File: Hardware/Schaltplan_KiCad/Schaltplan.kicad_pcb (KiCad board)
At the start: 2 copper layers, 153 x 153 mm, 62 parts, among them IC1 LD1085V50, J1 3-106505-2, J2 USB_B_Micro, J3 Conn_01x04_Pin, J4 Conn_01x02_Pin, U1 MCP2562-E-SN, U2 FT231XS, U3 ESP32-DEVKITC-32U, U5 PCA9306DCTR

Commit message: completed tracing of pcb
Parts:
- moved D4 7.00 mm to (157.4, 74.5), turned to 180 degrees
- moved R15 7.00 mm to (148.4, 74.5)
- moved R20 7.00 mm to (103.5, 66.5), turned to -90 degrees
- moved R21 7.00 mm to (96.5, 66.5), turned to -90 degrees
- moved D5 5.80 mm to (157.3, 68.2), turned to 180 degrees
- moved R16 5.80 mm to (148.3, 68.2)
- moved J2 1.07 mm to (163.2, 47.9)
- moved R1 0.81 mm to (143.1, 123.7), turned to 0 degrees
- turned D6 to 180 degrees
- turned D7 to 180 degrees
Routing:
- net +5V: track 0.00 -> 290.2 mm, vias 0 -> 2
- net +3V3: track 0.00 -> 195.8 mm
- net GNDREF: track 0.00 -> 111.6 mm, vias 0 -> 1
- net /FT231_RI: track 0.00 -> 101.3 mm, vias 0 -> 1
- net /ESP32_IO4: track 0.00 -> 96.9 mm, vias 0 -> 4
- net /ESP32_IO33: track 0.00 -> 90.4 mm, vias 0 -> 2
- net /FT231_RTS: track 0.00 -> 89.3 mm, vias 0 -> 1
- net /FT231_SLEEP: track 0.00 -> 85.3 mm, vias 0 -> 2
- net /FT231_CTS: track 0.00 -> 81.1 mm, vias 0 -> 1
- net /ESP32_SCL1: track 0.00 -> 72.9 mm, vias 0 -> 2
- net /CANL: track 0.00 -> 70.3 mm
- net /ESP32TX: track 0.00 -> 67.9 mm, vias 0 -> 1
- net /ESP32_IO13: track 0.00 -> 67.8 mm, vias 0 -> 1
- net /ESP32_SDA1: track 0.00 -> 66.4 mm, vias 0 -> 2
- net /ESP32_IO27: track 0.00 -> 65.6 mm, vias 0 -> 1
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- added copper zone on B.Cu, net GNDREF
- added copper zone on F.Cu, net GNDREF
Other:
- board text added: "BAT"
- board text added: "CAN Status LEDs"
- board text added: "DOWN"
- board text added: "ENTER"
- board text added: "OFF"
- board text added: "OFF/USB"
- board text added: "POWER"
- board text added: "UP"

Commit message: finishes PCB Design
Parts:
- removed BT2: 1049, battery_holder:BAT_1049
- removed C10, C9: 47pF, Capacitor_SMD:C_1812_4532Metric_Pad1.57x3.40mm_HandSolder
- removed C11: 10uF, Capacitor_SMD:C_1812_4532Metric_Pad1.57x3.40mm_HandSolder
- removed C13: C, Capacitor_SMD:C_1812_4532Metric_Pad1.57x3.40mm_HandSolder
- removed C3, C5, C7: 100nF, Capacitor_SMD:C_1812_4532Metric_Pad1.57x3.40mm_HandSolder
- removed C4, C6, C8: 4.7uF, Capacitor_SMD:C_1812_4532Metric_Pad1.57x3.40mm_HandSolder
- removed D1, D2: LED, LED:LED_OF-SMD3528WC
- removed IC1: LD1085V50, LDO:TO255P460X1020X2008-3P
- removed J2: USB_B_Micro, Connector_USB:USB_Micro-B_Amphenol_10103594-0001LF_Horizontal
- removed R20, R21, R22, R23: 10k, Resistor_SMD:R_2010_5025Metric_Pad1.40x2.65mm_HandSolder
- removed R6, R7: 270, Resistor_SMD:R_2010_5025Metric_Pad1.40x2.65mm_HandSolder
- removed S1, S2: 1103M2S3CQE2, switches:SW_1103M2S3CQE2
- removed U2: FT231XS, USB2UART:SOP63P600X175-20N
- C1: value 22uF -> 100nF; footprint Capacitor_SMD:C_1812_4532Metric_Pad1.57x3.40mm_HandSolder -> Capacitor_SMD:C_0603_1608Metric_Pad1.08x0.95mm_HandSolder
- C14, C15: footprint Capacitor_SMD:C_1812_4532Metric_Pad1.57x3.40mm_HandSolder -> Capacitor_SMD:C_0603_1608Metric_Pad1.08x0.95mm_HandSolder
- C2: value C -> 4.7uF; footprint Capacitor_SMD:C_1812_4532Metric_Pad1.57x3.40mm_HandSolder -> Capacitor_SMD:C_0603_1608Metric_Pad1.08x0.95mm_HandSolder
- J1, U1, U3: moved to B.Cu
- R1: value R -> 120R; footprint Resistor_SMD:R_2010_5025Metric_Pad1.40x2.65mm_HandSolder -> Resistor_SMD:R_0603_1608Metric_Pad0.98x0.95mm_HandSolder
- R10, R11, R12, R13, R14, R15, R16, R17, R18, R19, R8, R9: footprint Resistor_SMD:R_2010_5025Metric_Pad1.40x2.65mm_HandSolder -> Resistor_SMD:R_0603_1608Metric_Pad0.98x0.95mm_HandSolder
- R2, R3: value 27R -> 10k; footprint Resistor_SMD:R_2010_5025Metric_Pad1.40x2.65mm_HandSolder -> Resistor_SMD:R_0603_1608Metric_Pad0.98x0.95mm_HandSolder
- R4, R5: value R -> 10k; footprint Resistor_SMD:R_2010_5025Metric_Pad1.40x2.65mm_HandSolder -> Resistor_SMD:R_0603_1608Metric_Pad0.98x0.95mm_HandSolder
- moved D3 177.9 mm to (56.3, 178.2), turned to 0 degrees
- moved D5 141.3 mm to (86.1, 190.2), turned to 0 degrees
- moved D4 140.5 mm to (77.8, 190.2), turned to 0 degrees
- moved R8 130.8 mm to (87.5, 147.2), turned to -90 degrees
- moved D6 121.6 mm to (103.7, 190.0), turned to 0 degrees
- moved D7 120.3 mm to (95.0, 190.2), turned to 0 degrees
- moved C1 117.0 mm to (50.3, 93.6), turned to 90 degrees
- moved J1 94.9 mm to (60.3, 127.3)
- moved C2 94.8 mm to (55.3, 93.6), turned to 90 degrees
- moved R16 92.9 mm to (99.6, 147.2), turned to -90 degrees
- moved R15 90.8 mm to (94.1, 147.2), turned to -90 degrees
- moved R11 90.5 mm to (67.8, 171.0)
- moved R14 82.3 mm to (67.8, 166.2)
- moved J4 79.2 mm to (66.4, 134.2), turned to 180 degrees
- moved R1 76.7 mm to (66.4, 125.3), turned to 90 degrees
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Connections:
- C14 pad 1: +5V -> +3V3
- C15 pad 1: +5V -> +3V3
- C2 pad 1: /FT231_3V3_OUT -> +5V
- D6 pad 1: /ESP32_IO13 -> /ESP32_IO19
- D7 pad 1: /ESP32_IO14 -> /ESP32_IO13
- R12 pad 2: /ESP32_IO5 -> /ESP32_IO18
- R2 pad 1: /FT231_USBDM -> +5V
- R2 pad 2: /USBDM -> /ESP32_SCL1
- R3 pad 1: /USBDP -> +5V
- R3 pad 2: /FT231_USBDP -> /DISPLAY_SCL2
- R4 pad 1: /FT231_RX -> +5V
- R4 pad 2: /ESP32TX -> /DISPLAY_SDA2
- R5 pad 1: /FT231_TX -> +5V
- R5 pad 2: /ESP32RX -> /ESP32_SDA1
- U3 pad 12: /ESP32_IO14 -> unconnected-(U3-IO14-Pad12)
- U3 pad 27: /ESP32RX -> unconnected-(U3-IO16-Pad27)
- U3 pad 28: /ESP32TX -> unconnected-(U3-IO17-Pad28)
- U3 pad 29: /ESP32_IO5 -> unconnected-(U3-IO5-Pad29)
- U3 pad 30: /FT231_CTS -> /ESP32_IO18
- U3 pad 31: /FT231_RTS -> /ESP32_IO19
- U3 pad 37: /FT231_RI -> unconnected-(U3-IO23-Pad37)
- U3 pad 7: /FT231_SLEEP -> unconnected-(U3-IO32-Pad7)
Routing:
- net /ESP32_IO19: track 0.00 -> 122.8 mm, vias 0 -> 1
- net /FT231_RI: track 101.3 -> 0.00 mm, vias 1 -> 0
- net +5V: track 290.2 -> 192.7 mm, vias 2 -> 0
- net /FT231_RTS: track 89.3 -> 0.00 mm, vias 1 -> 0
- net /ESP32_IO18: track 0.00 -> 88.3 mm, vias 0 -> 1
- net /FT231_SLEEP: track 85.3 -> 0.00 mm, vias 2 -> 0
- net /FT231_CTS: track 81.1 -> 0.00 mm, vias 1 -> 0
- net GNDREF: track 111.6 -> 36.6 mm, vias 1 -> 2
- net /ESP32TX: track 67.9 -> 0.00 mm, vias 1 -> 0
- net /ESP32_IO14: track 64.8 -> 0.00 mm, vias 2 -> 0
- net /ESP32_IO13: track 67.8 -> 129.4 mm, vias 1 -> 0
- net /ESP32RX: track 61.5 -> 0.00 mm, vias 1 -> 0
- net /ESP32_IO5: track 61.0 -> 0.00 mm
- net /ESP32_IO4: track 96.9 -> 151.6 mm, vias 4 -> 0
- net Net-(D4-A): track 5.17 -> 55.0 mm, vias 0 -> 2
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- removed copper zone on B.Cu, net GNDREF
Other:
- board size 153 x 153 mm -> 72 x 138 mm
- board text removed: "BAT"
- board text removed: "CAN Status LEDs"
- board text removed: "DOWN"
- board text removed: "Display"
- board text removed: "ENTER"
- board text removed: "OFF"
- board text removed: "OFF/USB"
- board text removed: "POWER"
- board text removed: "UP"

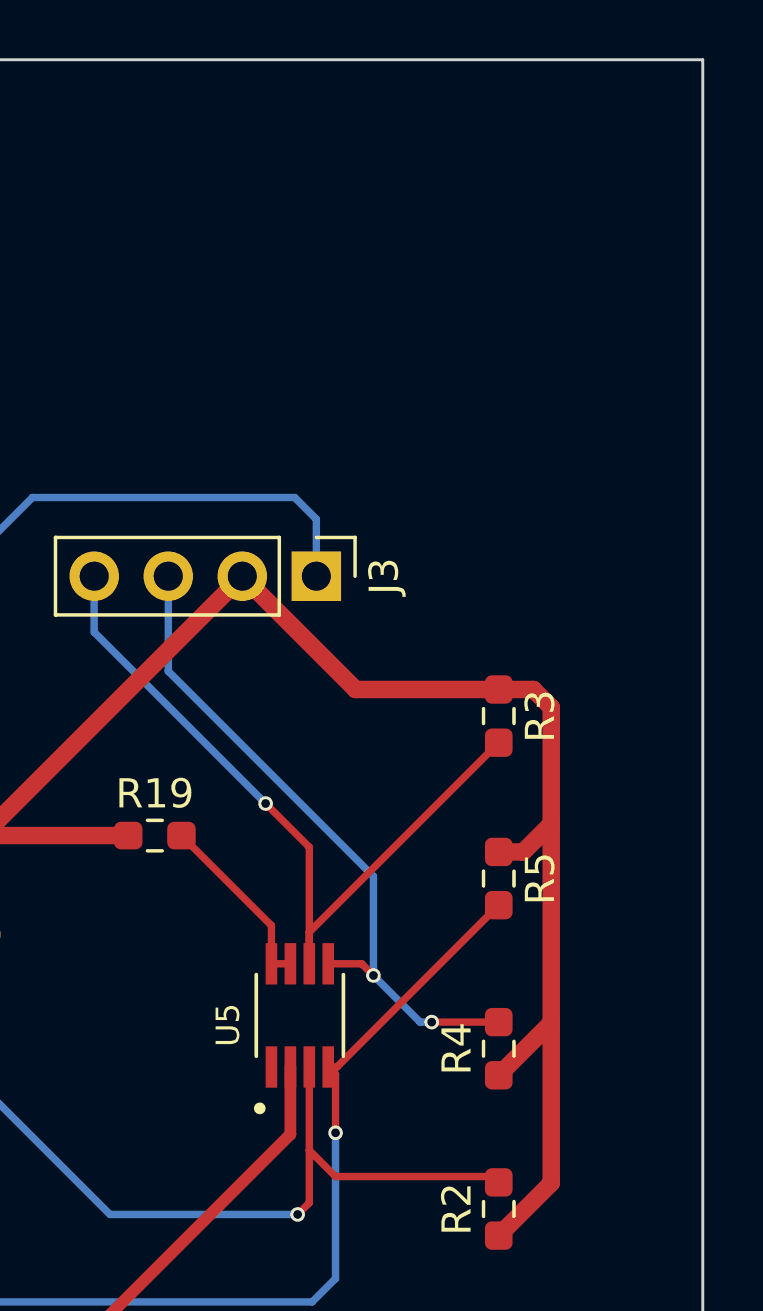
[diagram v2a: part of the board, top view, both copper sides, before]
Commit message: verbesserungen und 4te Bohrung und bestellt
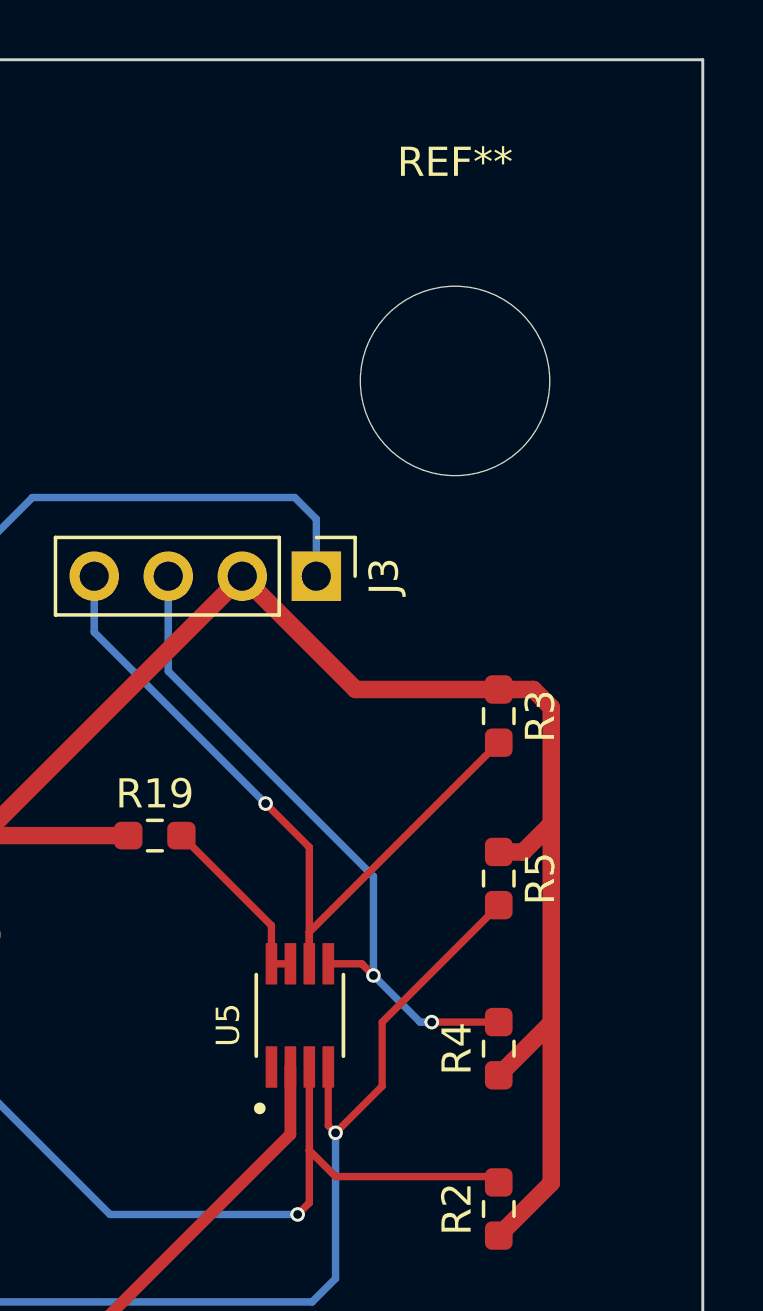
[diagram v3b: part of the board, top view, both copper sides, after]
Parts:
- added REF**: MountingHole_6.5mm, MountingHole:MountingHole_6.5mm, F.Cu at (111.0, 67.0)
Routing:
- net /ESP32_SDA1: track 48.0 -> 50.0 mm
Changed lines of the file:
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@@
   )
   (paper "A4")
+  (title_block
+    (comment 4 "AISLER Project ID: BMIDAAET")
+  )
   (layers
     (0 "F.Cu" signal)
@@
       (rotate (xyz 0 0 0))
     )
+  )
+  (footprint "MountingHole:MountingHole_6.5mm" (layer "F.Cu")
+    (at 111 67)
+    (descr "Mounting Hole 6.5mm, no annular")
+    (tags "mounting hole 6.5mm no annular")
+    (attr exclude_from_pos_files exclude_from_bom)
+    (fp_text reference "REF**" (at 0 -7.5) (layer "F.SilkS")
+        (effects (font (size 1 1) (thickness 0.15)))
+    )
+    (fp_text value "MountingHole_6.5mm" (at 0 7.5) (layer "F.Fab")
+        (effects (font (size 1 1) (thickness 0.15)))
+    )
+    (fp_text user "${REFERENCE}" (at 0 0) (layer "F.Fab")
+        (effects (font (size 1 1) (thickness 0.15)))
+    )
+    (fp_circle (center 0 0) (end 6.5 0)
+      (stroke (width 0.15) (type solid)) (fill none) (layer "Cmts.User"))
+    (fp_circle (center 0 0) (end 6.75 0)
+      (stroke (width 0.05) (type solid)) (fill none) (layer "F.CrtYd"))
+    (pad "" np_thru_hole circle (at 0 0) (size 6.5 6.5) (drill 6.5) (layers "*.Cu" "*.Mask"))
   )
   (footprint "Connector_PinHeader_2.54mm:PinHeader_1x02_P2.54mm_Vertical" (layer "F.Cu")
@@
   (segment (start 105.35 87) (end 104.7 87) (width 0.254) (layer "F.Cu") (net 35))
   (segment (start 104.7 87) (end 104.7 85.6875) (width 0.254) (layer "F.Cu") (net 35))
-  (segment (start 112.5 84.9875) (end 106.9475 90.54) (width 0.254) (layer "F.Cu") (net 36))
-  (segment (start 106.9475 90.54) (end 106.65 90.54) (width 0.254) (layer "F.Cu") (net 36))
-  (segment (start 106.9 92.8) (end 106.9 90.79) (width 0.254) (layer "F.Cu") (net 36))
-  (segment (start 106.9 90.79) (end 106.65 90.54) (width 0.254) (layer "F.Cu") (net 36))
+  (segment (start 106.65 92.55) (end 106.9 92.8) (width 0.25) (layer "F.Cu") (net 36))
+  (segment (start 108.5 91.2) (end 108.5 89) (width 0.25) (layer "F.Cu") (net 36))
+  (segment (start 112.5 85) (end 112.5 84.9875) (width 0.25) (layer "F.Cu") (net 36))
+  (segment (start 108.5 89) (end 112.5 85) (width 0.25) (layer "F.Cu") (net 36))
+  (segment (start 106.9 92.8) (end 108.5 91.2) (width 0.25) (layer "F.Cu") (net 36))
+  (segment (start 106.65 90.54) (end 106.65 92.55) (width 0.25) (layer "F.Cu") (net 36))
   (via (at 106.9 92.8) (size 0.5) (drill 0.3) (layers "F.Cu" "B.Cu") (net 36))
   (segment (start 106.9 97.8) (end 106.1 98.6) (width 0.254) (layer "B.Cu") (net 36))
